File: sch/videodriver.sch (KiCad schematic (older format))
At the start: 48 parts, among them IC21 74HCT245, IC22 P8X32A-D40, IC23 24C512

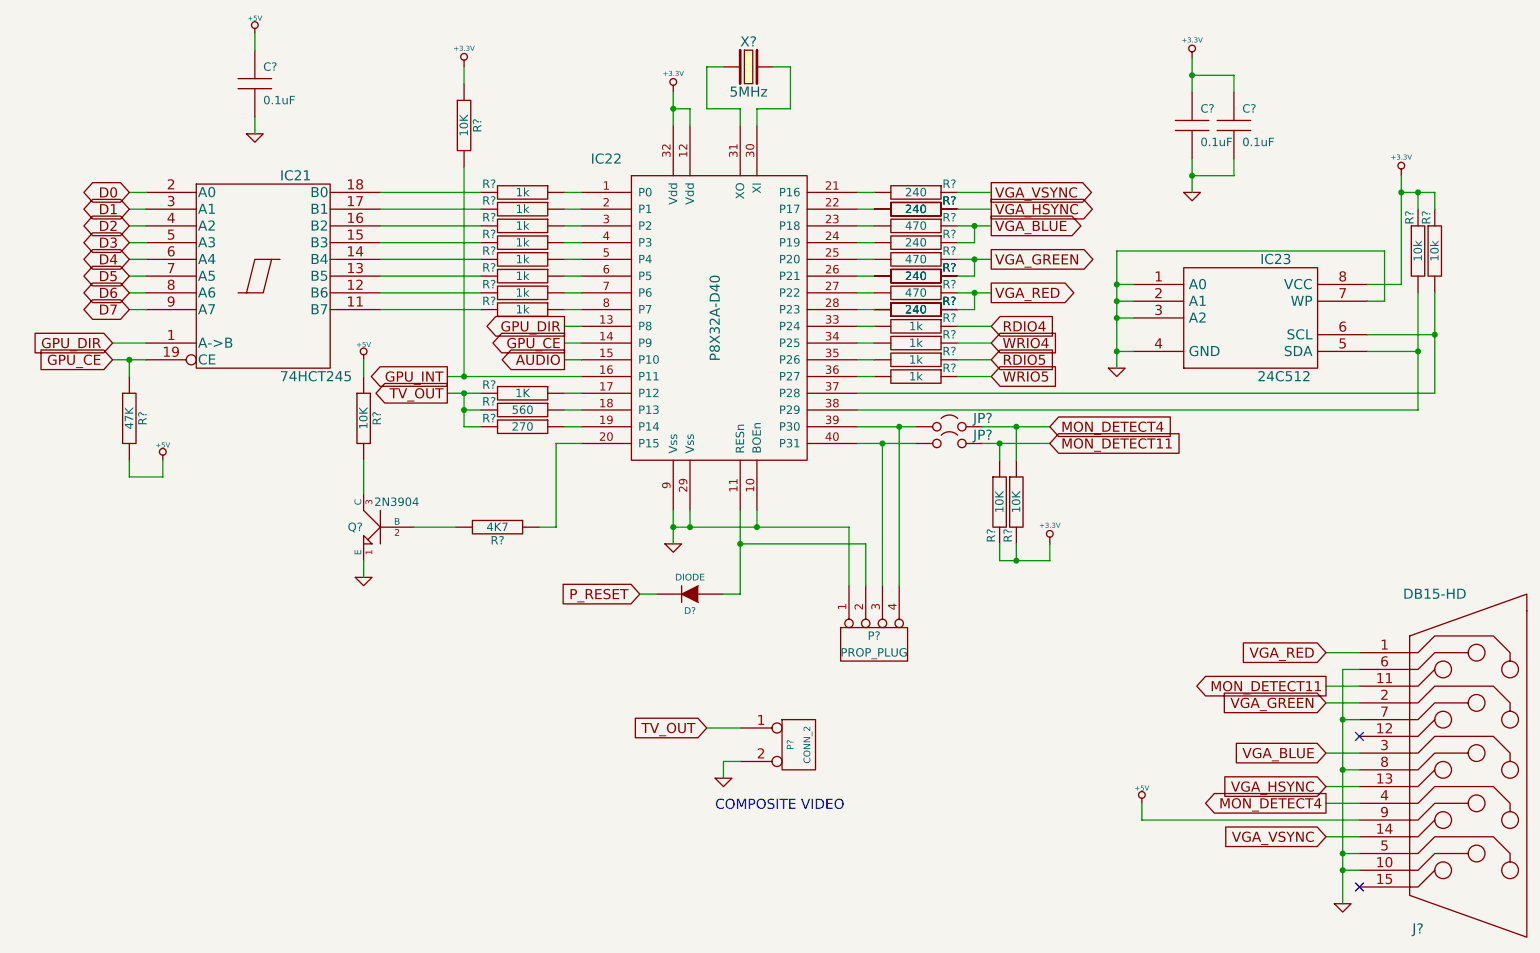
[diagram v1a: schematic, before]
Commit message: Updated the code and circuit diagrams for first boot from banked RAM.
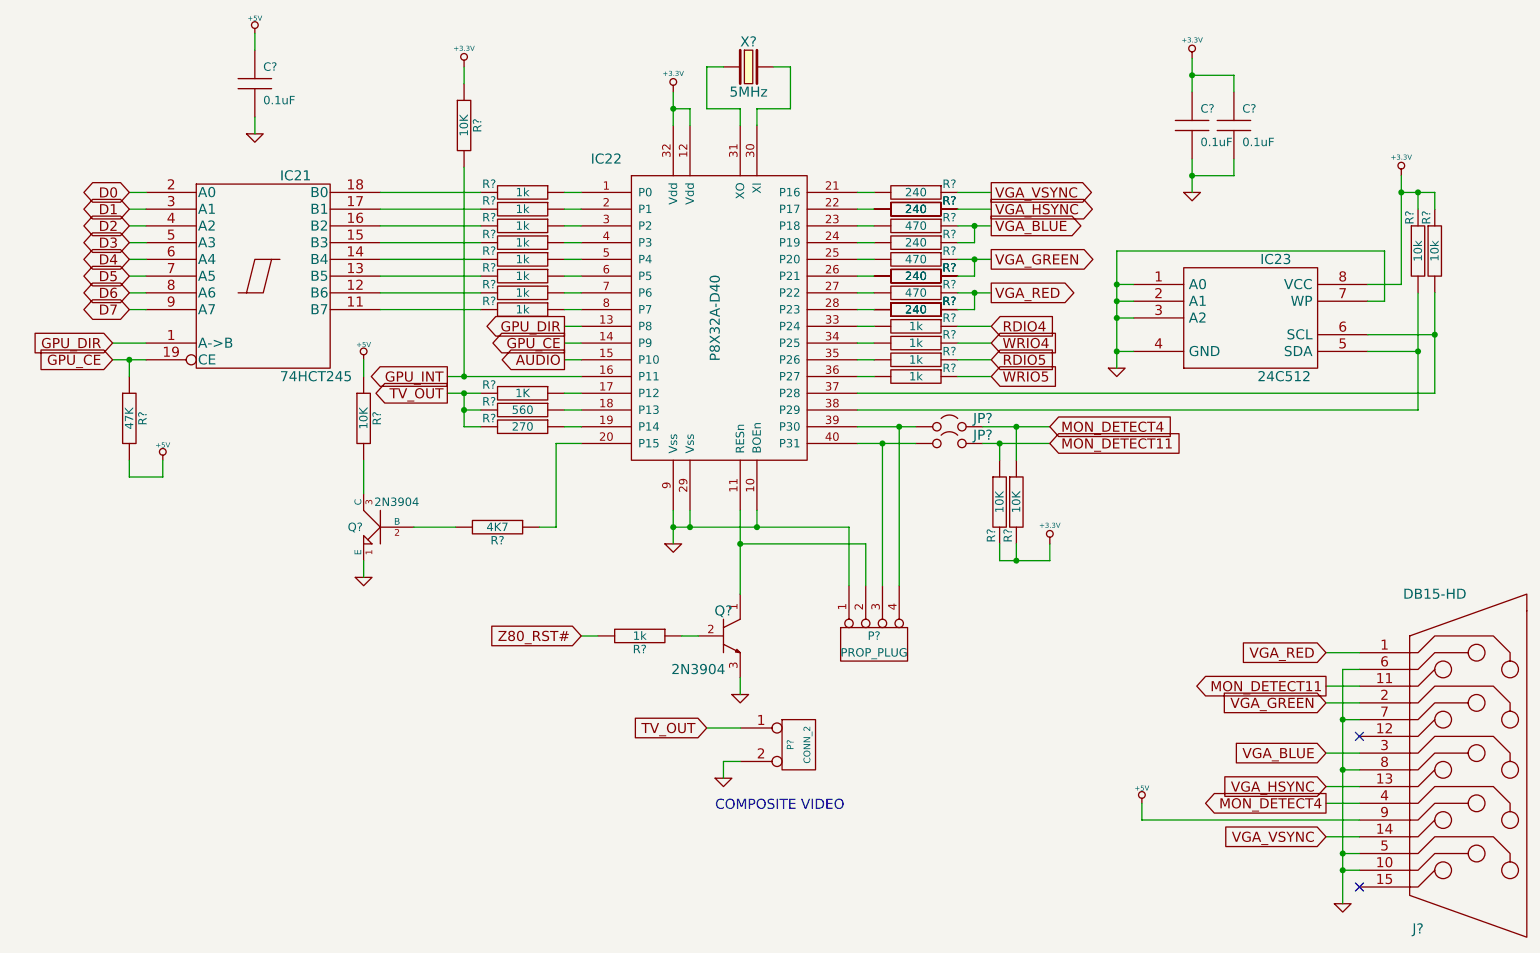
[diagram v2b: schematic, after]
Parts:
- removed D?: DIODE, symbol DIODE
- added Q?: 2N3904, symbol 2N3904
- added R?: 1k, symbol R
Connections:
- net GND: now also Q?.3 (E)
- net at IC22.11 (RESn), P?.2 (P2): now also Q?.1 (C)
- new net: Q?.2 (B), R?.1
- new net Z80_RST#: R?.2
